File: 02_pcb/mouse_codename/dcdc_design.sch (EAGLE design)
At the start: 2 parts, among them IC1 STM32F405RGT6LQFP64

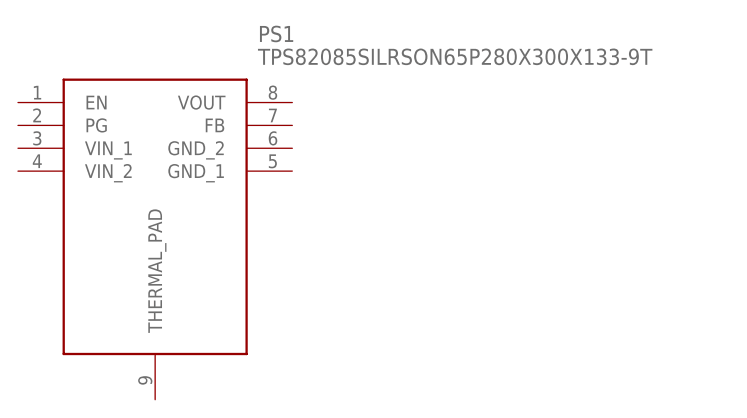
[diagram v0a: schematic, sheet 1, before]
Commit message: eagle board layout synced with fuison 360
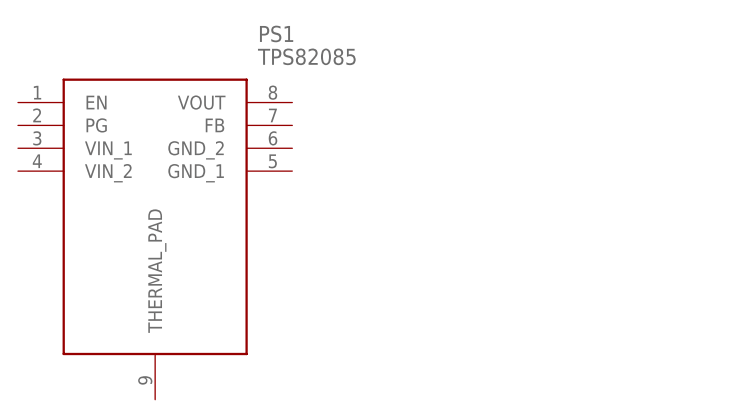
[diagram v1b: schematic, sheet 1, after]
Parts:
- added IC2: DRV8836, SamacSys_Parts:DRV8836DSSR
- IC1: value STM32F405RGT6LQFP64 -> STM32F405RG
- PS1: value TPS82085SILRSON65P280X300X133-9T -> TPS82085
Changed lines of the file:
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@@
 </classes>
 <parts>
-<part name="PS1" library="SamacSys_Parts" deviceset="TPS82085SILR" device="SON65P280X300X133-9T" package3d_urn="urn:adsk.eagle:package:8852109/1"/>
-<part name="IC1" library="SamacSys_Parts" deviceset="STM32F405RGT6" device="LQFP64" package3d_urn="urn:adsk.eagle:package:8852219/1"/>
+<part name="PS1" library="SamacSys_Parts" deviceset="TPS82085SILR" device="SON65P280X300X133-9T" package3d_urn="urn:adsk.eagle:package:8852109/1" value="TPS82085"/>
+<part name="IC1" library="SamacSys_Parts" deviceset="STM32F405RGT6" device="LQFP64" package3d_urn="urn:adsk.eagle:package:8852219/1" value="STM32F405RG"/>
+<part name="IC2" library="SamacSys_Parts" deviceset="DRV8836DSSR" device="" value="DRV8836"/>
 </parts>
 <sheets>
@@
 </plain>
 <instances>
+<instance part="IC2" gate="G$1" x="20.32" y="66.04" smashed="yes">
+<attribute name="NAME" x="57.15" y="73.66" size="1.778" layer="95" align="center-left"/>
+<attribute name="VALUE" x="57.15" y="71.12" size="1.778" layer="96" align="center-left"/>
+</instance>
 </instances>
 <busses>
